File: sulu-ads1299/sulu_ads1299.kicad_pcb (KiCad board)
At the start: 2 copper layers, 32.5 x 42.8 mm, 88 parts, among them J1 Conn_01x08, J10 through_hole, J11 through_hole, J12 through_hole, J13 through_hole, J14 through_hole, J15 through_hole, J16 through_hole, J17 through_hole, J18 through_hole, J19 through_hole, J20 through_hole, J21 through_hole, J22 through_hole, J3 Conn_01x02, J4 Conn_02x05_Odd_Even, J5 through_hole, J6 through_hole, J7 through_hole, J8 through_hole, J9 through_hole, SW1 SW_DIP_x02, U1 TPS62222DDCT, U2 S-85S1AB11-I6T1U, U3 LM2775DSG, U4 ADS1299_TQFP-64, U5 scum3

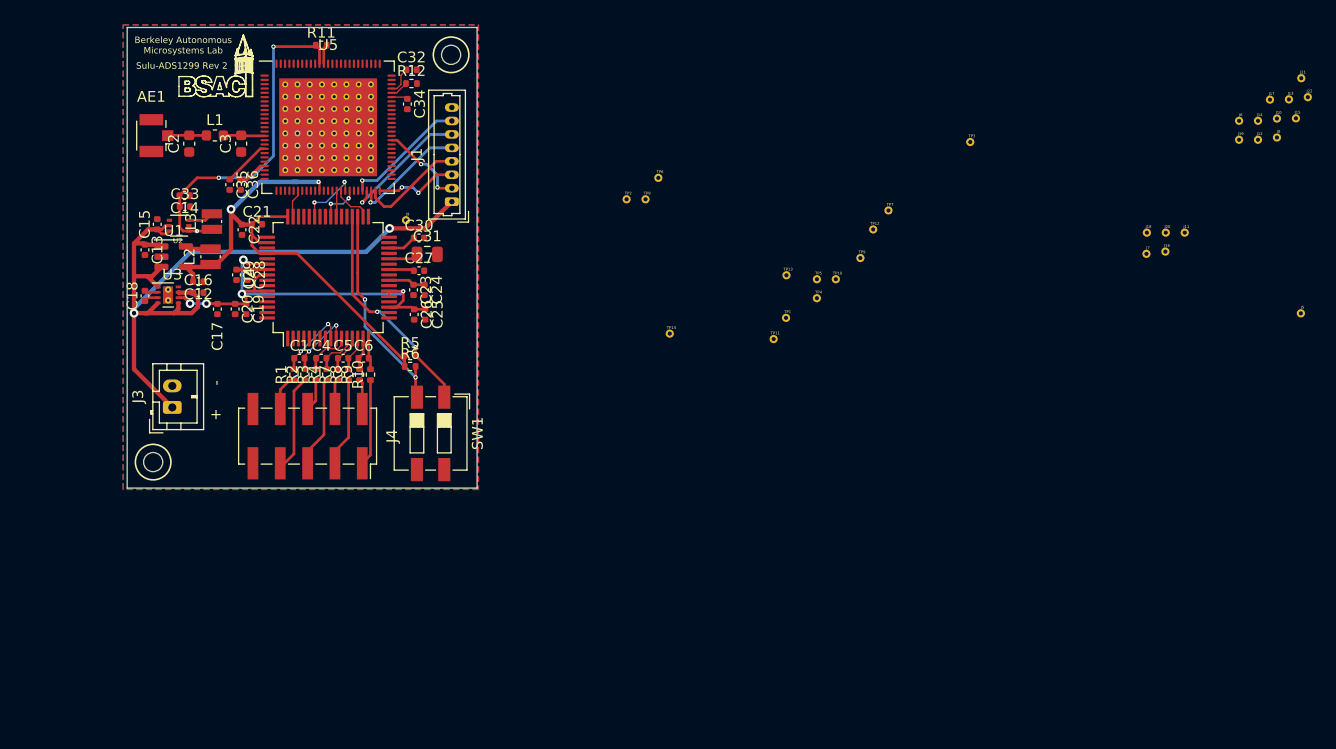
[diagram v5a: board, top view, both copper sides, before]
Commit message: Silkscreen cleaned, reduced TP footprint #, post design review
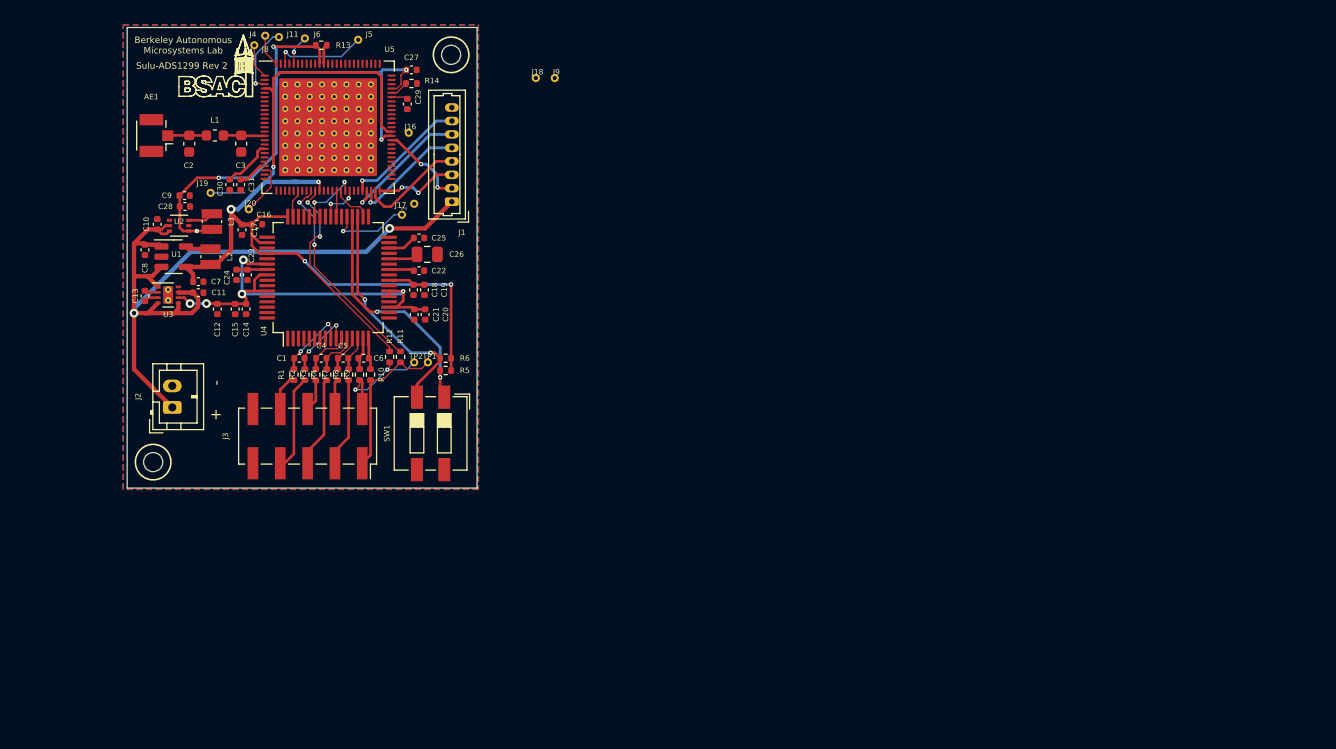
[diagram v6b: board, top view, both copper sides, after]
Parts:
- removed J12, J14, J15: through_hole, SCUM:through_hole
- removed the J16 at (181.4, 71.9)
- removed the J17 at (191.2, 57.8)
- removed the J5 at (194.0, 77.6)
- removed the J9 at (110.9, 69.0)
- removed TP10, TP11, TP12, TP13, TP14, TP4, TP5, TP6, TP7, TP8, TP9: TestPoint, SCUM:through_hole
- added R11: 0, Resistor_SMD:R_0402_1005Metric, F.Cu at (110.4, 81.7)
- added R12: 0, Resistor_SMD:R_0402_1005Metric, F.Cu at (109.3, 81.7)
- moved J19 101.9 mm to (92.7, 66.4)
- moved J20 99.0 mm to (96.3, 67.9)
- moved J8 95.3 mm to (96.8, 52.7)
- moved J11 94.0 mm to (99.1, 51.9)
- moved J4 90.8 mm to (97.8, 51.8)
- moved J6 90.8 mm to (101.5, 52.1)
- moved J17 76.9 mm to (111.6, 67.4)
- moved J5 75.9 mm to (106.4, 52.2)
- moved J16 69.2 mm to (111.1, 60.8)
- moved J9 60.3 mm to (124.7, 55.8)
- moved J18 60.3 mm to (122.9, 55.8)
- moved TP3 53.2 mm to (110.5, 68.5)
- moved TP1 33.5 mm to (112.9, 82.2)
- moved TP2 24.9 mm to (111.6, 82.2)
- moved R5 3.59 mm to (114.6, 82.9), turned to 180 degrees
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- renumbered C15 to C10, C16 to C11, C17 to C12, C18 to C13, C19 to C14, C20 to C15, C21 to C16, C22 to C17, C23 to C18, C24 to C19, C25 to C20, C26 to C21, C27 to C22, C28 to C23, C29 to C24, C30 to C25, C31 to C26, C32 to C27, C33 to C28, C34 to C29, C35 to C30, C36 to C31, C12 to C7, C13 to C8, C14 to C9, J13 to J11, J18 to J16, J19 to J17, J20 to J18, J21 to J19, J3 to J2, J22 to J20, J4 to J3, J6 to J4, J7 to J5, J8 to J6, J10 to J8, J11 to J9, R11 to R13, R12 to R14
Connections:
- TP1 pad 1: /SCUM_GPIO2 -> /ADS_IN1P_CONN
- TP2 pad 1: /SCUM_GPIO3 -> /ADS_IN1N_CONN
- TP3 pad 1: /SCUM_GPIO4 -> Net-(TP3-Pad1)
- U4 pad 37: Net-(J5-Pad1) (its old number) -> Net-(TP3-Pad1)
- U5 pad 63: Net-(J17-Pad1) (its old number) -> unconnected-(U5-Pad63)
- U5 pad 64: Net-(J16-Pad1) (its old number) -> unconnected-(U5-Pad64)
- U5 pad 65: Net-(J15-Pad1) -> unconnected-(U5-Pad65)
- U5 pad 67: Net-(J14-Pad1) -> unconnected-(U5-Pad67)
- U5 pad 73: Net-(J12-Pad1) -> unconnected-(U5-Pad73)
- U5 pad 75: Net-(J9-Pad1) (its old number) -> unconnected-(U5-Pad75)
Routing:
- net +1.8V_REG: track 50.7 -> 86.3 mm, vias 2 -> 5
- net +1.1V_REG: track 35.0 -> 55.7 mm, vias 3 -> 5
- net /SCUM_GPIO6: track 0.00 -> 19.5 mm, vias 0 -> 2
- net /SCUM_GPIO7: track 0.00 -> 19.3 mm, vias 0 -> 2
- net Net-(J5-Pad1): track 0.00 -> 8.65 mm, vias 0 -> 1
- net /ADS_IN1N_CONN: track 2.79 -> 11.1 mm, vias 0 -> 2
- net Net-(TP3-Pad1): track 0.00 -> 7.58 mm, vias 0 -> 1
- net /ADS_IN1P_CONN: track 8.04 -> 14.5 mm
- net Net-(J11-Pad1): track 0.00 -> 6.39 mm, vias 0 -> 1
- net Net-(J20-Pad1): track 0.00 -> 5.01 mm
- net Net-(J8-Pad1): track 0.00 -> 3.22 mm
- net Net-(J19-Pad1): track 0.00 -> 3.18 mm
- net Net-(J4-Pad1): track 0.00 -> 3.04 mm
- net Net-(J6-Pad1): track 0.00 -> 2.79 mm, vias 0 -> 1
- net /~{ADS_PWDN}: track 20.1 -> 22.3 mm
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
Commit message: Sulu-ADS1299 rev2 commit before changing 1.1V regulator
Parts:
- removed J18, J19, J9: through_hole, SCUM:through_hole
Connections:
- U5 pad 2: Net-(J9-Pad1) -> unconnected-(U5-Pad2)
- U5 pad 20: Net-(J18-Pad1) -> unconnected-(U5-Pad20)
- U5 pad 21: Net-(J19-Pad1) -> unconnected-(U5-Pad21)
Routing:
- net GND: track 0.00 -> 21.9 mm, vias 0 -> 15
- net Net-(J17-Pad1): track 0.00 -> 6.55 mm, vias 0 -> 1
- net Net-(J16-Pad1): track 0.00 -> 4.02 mm, vias 0 -> 1
- net Net-(J19-Pad1): track 3.18 -> 0.00 mm
- net +1.8V_REG: track 86.3 -> 85.8 mm, vias 5 -> 7
- net +1.1V_REG: track 55.7 -> 55.9 mm, vias 5 -> 4
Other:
- board text added: "Sulu-ADS1299 Rev.2"
- board text removed: "Sulu-ADS1299 Rev 2"

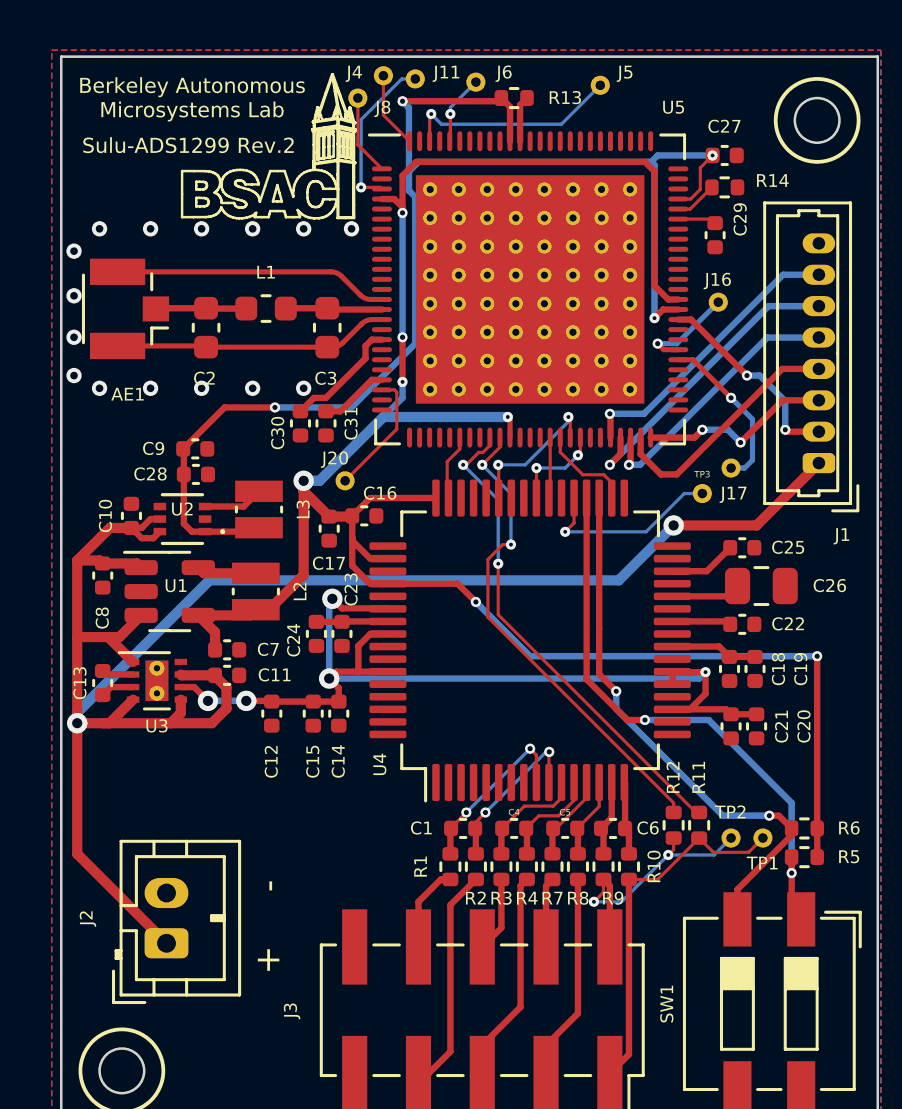
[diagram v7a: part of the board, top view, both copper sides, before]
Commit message: BOM adjustments, protection Zener diodes, JLCPCB fab files
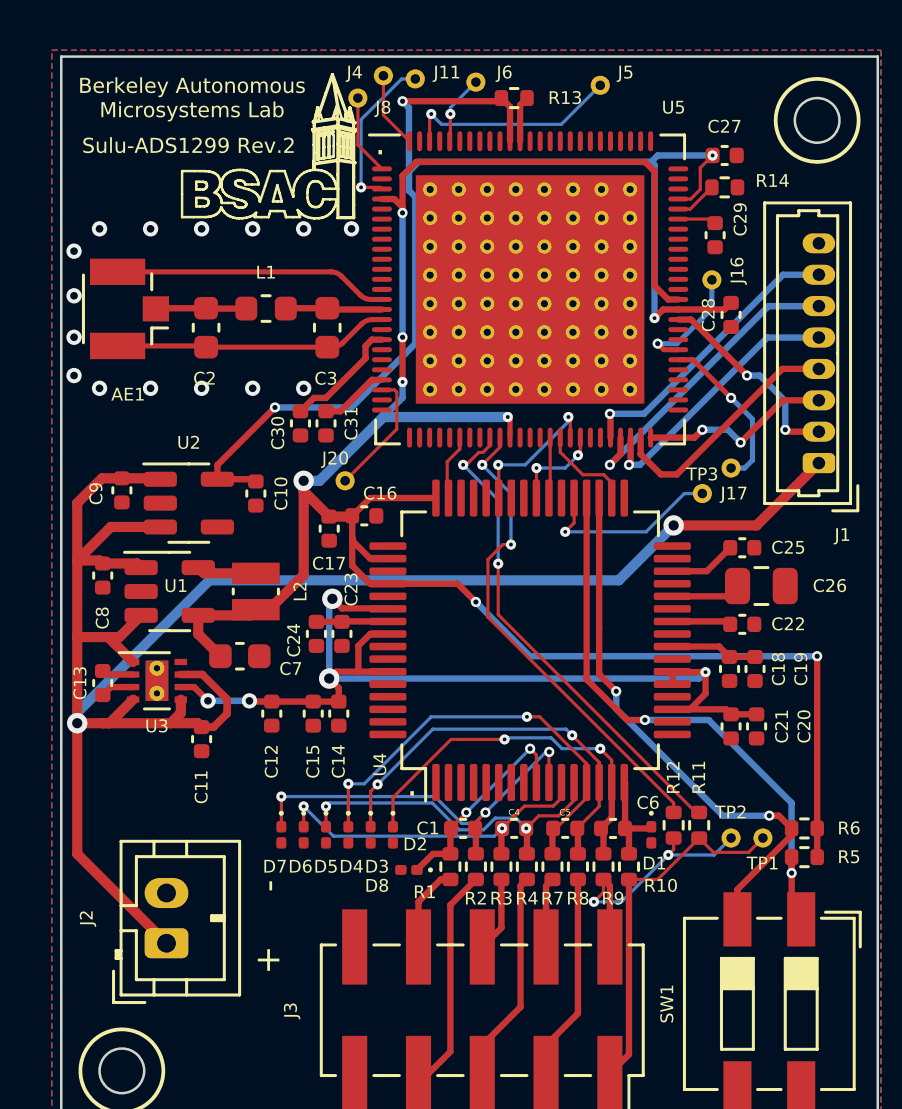
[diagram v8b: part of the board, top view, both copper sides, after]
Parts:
- removed L3: 2.2 uH, Inductor_SMD:L_Wuerth_MAPI-2010
- added D1: GDZ5V1LP3-7, Diode_SMD:D_0201_0603Metric, F.Cu at (108.5, 82.0)
- added D2: GDZ5V1LP3-7, Diode_SMD:D_0201_0603Metric, F.Cu at (98.2, 82.0)
- added D3: GDZ5V1LP3-7, Diode_SMD:D_0201_0603Metric, F.Cu at (97.3, 82.0)
- added D4: GDZ5V1LP3-7, Diode_SMD:D_0201_0603Metric, F.Cu at (96.4, 82.0)
- added D5: GDZ5V1LP3-7, Diode_SMD:D_0201_0603Metric, F.Cu at (95.5, 82.0)
- added D6: GDZ5V1LP3-7, Diode_SMD:D_0201_0603Metric, F.Cu at (94.6, 82.0)
- added D7: GDZ5V1LP3-7, Diode_SMD:D_0201_0603Metric, F.Cu at (93.7, 82.0)
- added D8: GDZ5V1LP3-7, Diode_SMD:D_0201_0603Metric, F.Cu at (98.8, 83.4)
- C10, C9: value 10 uF -> 0.1 uF
- C2, C3: value 22 uF -> NP
- C7: footprint Capacitor_SMD:C_0402_1005Metric -> Capacitor_SMD:C_0603_1608Metric
- L1: value 2.2 uH -> NP
- U2: value S-85S1AB11-I6T1U -> TLV71311PDBV; footprint downloaded_libs:SOFL50P180X50-6N -> Package_TO_SOT_SMD:SOT-23-5
- moved C28 22.2 mm to (111.6, 61.3), turned to -90 degrees
- moved C10 5.03 mm to (92.7, 68.5), turned to -90 degrees
- moved C9 3.36 mm to (87.4, 68.3), turned to -90 degrees
- moved C11 2.74 mm to (90.6, 78.2), turned to -90 degrees
- moved J16 0.92 mm to (110.9, 59.9)
- moved U2 0.68 mm to (90.0, 68.8), turned to 0 degrees
- moved C7 0.57 mm to (92.1, 74.9)
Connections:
- C10 pad 1: +EXT_BAT -> +1.1V_REG
- C9 pad 1: GND -> +EXT_BAT
- C9 pad 2: +1.1V_REG -> GND
- U2 pad 1: +1.1V_REG -> +EXT_BAT
- U2 pad 3: Net-(L3-Pad2) -> +EXT_BAT
- U2 pad 4: GND -> unconnected-(U2-Pad4)
- U2 pad 5: +EXT_BAT -> +1.1V_REG
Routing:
- net /ADS_IN2N: track 3.48 -> 17.3 mm, vias 0 -> 2
- net /ADS_IN2P: track 3.22 -> 16.1 mm, vias 0 -> 2
- net /ADS_IN1N: track 3.06 -> 15.2 mm, vias 0 -> 2
- net /ADS_IN4P: track 6.59 -> 16.5 mm, vias 2 -> 3
- net /ADS_IN3P: track 4.11 -> 13.8 mm, vias 0 -> 2
- net /ADS_IN3N: track 4.51 -> 13.8 mm, vias 0 -> 2
- net +EXT_BAT: track 74.9 -> 79.4 mm
- net +1.1V_REG: track 55.9 -> 53.0 mm
- net Net-(L3-Pad2): track 2.40 -> 0.00 mm
- net /ADS_IN4N: track 6.95 -> 8.55 mm
- net /ADS_IN1P: track 2.92 -> 3.99 mm
- net Net-(J16-Pad1): track 4.02 -> 4.80 mm
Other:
- board text added: "."
